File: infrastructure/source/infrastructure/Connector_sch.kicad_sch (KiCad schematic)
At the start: 19 parts, among them J1 213227-1210, J12 TFM-105-02-L-DH, J13 TFM-103-02-L-DH, J2 TFM-103-02-L-DH, J3 TFM-108-02-X-DH-XX, J4 1-406541-5, J5 1-406541-5, J6 1-406541-5, J7 GSB1C211110DS1HR, J8 GSB1C211110DS1HR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

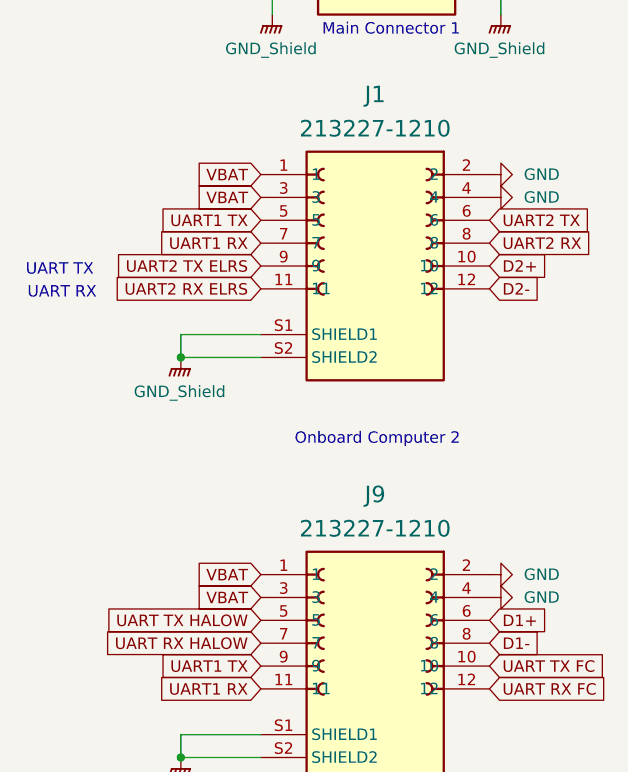
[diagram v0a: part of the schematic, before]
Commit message: Update VBAT net
connection VBAT net to +5V
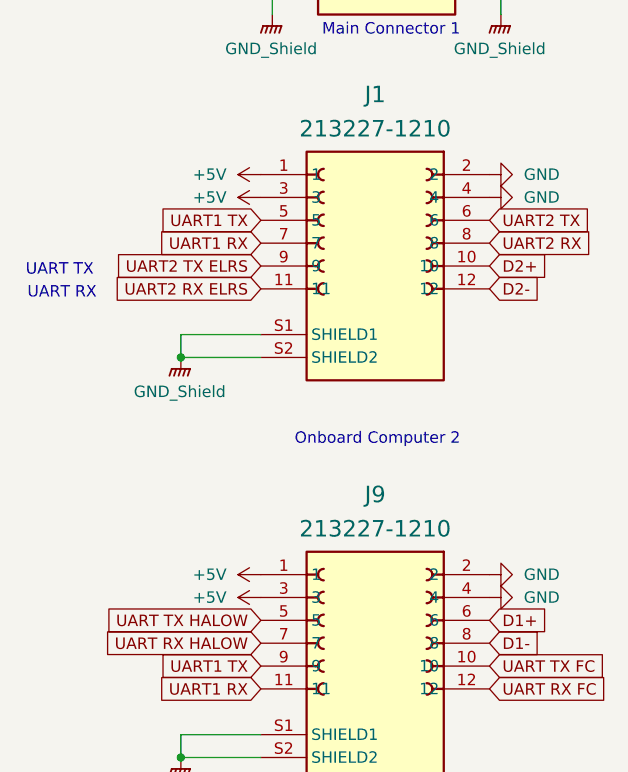
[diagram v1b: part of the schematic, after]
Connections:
- net +5V: now also J1.1, J1.3, J9.1, J9.3
- net VBAT: no longer J1.1, J1.3, J9.1, J9.3
